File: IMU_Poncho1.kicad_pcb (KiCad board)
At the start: 2 copper layers, 41 x 61 mm, 11 parts, among them J1 Conn_01x06_Female, U1 MPU-9250

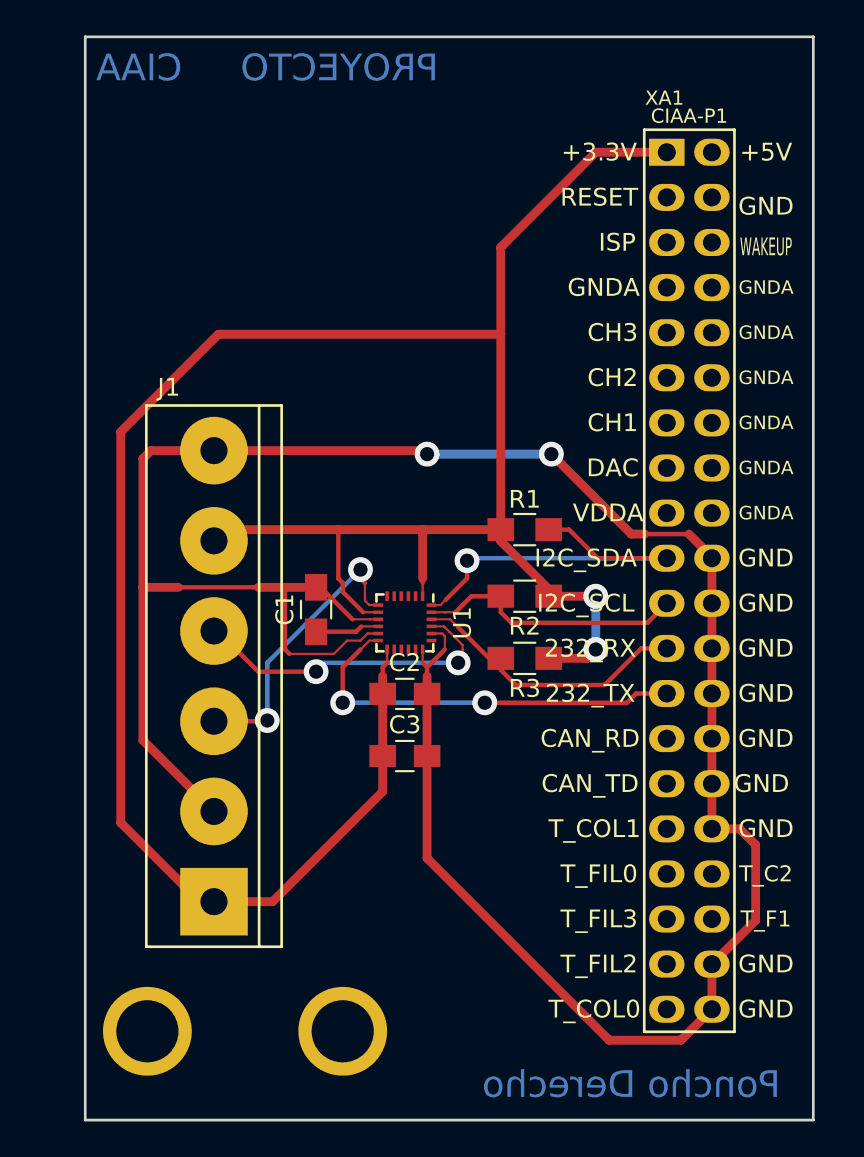
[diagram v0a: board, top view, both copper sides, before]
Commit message: Correccion del conector del barometro y se lo coloca separado del IMU. Dibujo 3D
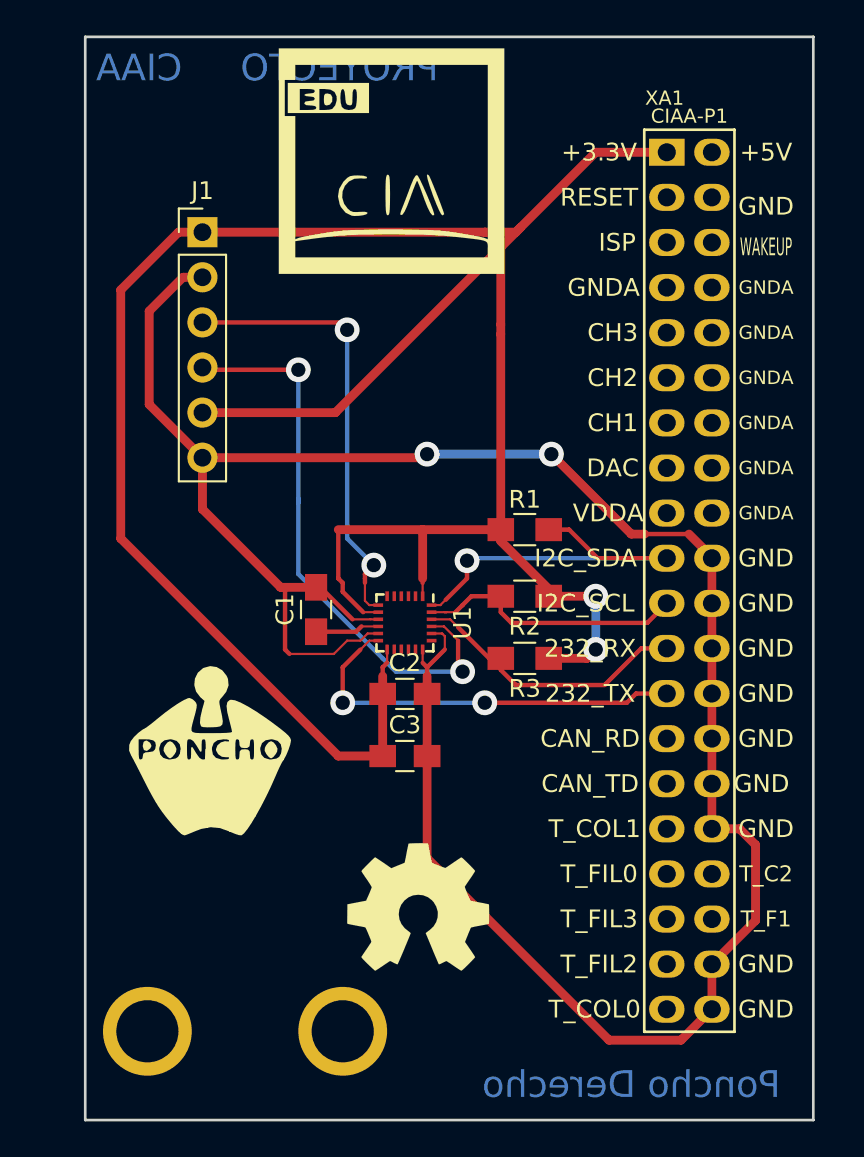
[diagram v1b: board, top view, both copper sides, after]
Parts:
- added G1: LOGO, Poncho_Esqueleto:Logo_Poncho, F.Cu at (132.5, 125.2)
- added G2: Logo_OSHWA, Poncho_Esqueleto:Logo_OSHWA, F.Cu at (144.2, 134.0)
- added G3: Logo_EDU-CIAA, Poncho_Esqueleto:Logo_EDU-CIAA, F.Cu at (142.8, 92.0)
- J1: footprint Poncho_Modelos:bornier6 -> Pin_Headers:Pin_Header_Straight_1x06_Pitch2.54mm
- moved J1 25.0 mm to (132.1, 96.0), turned to 0 degrees
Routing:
- net Net-(J1-Pad4): track 18.3 -> 32.4 mm
- net GND: track 143.9 -> 133.6 mm
- net Net-(J1-Pad3): track 16.4 -> 25.3 mm
- net +3V3: track 140.0 -> 144.4 mm
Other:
- net class Default: clearance 0.2 -> 0.125
- rule trace_clearance: 0.2 -> 0.125

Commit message: Corrigiendo seguimiento de archivos, borrando del grupo
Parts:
- added REF**: Fiducial_Modern_CopperTop, Fiducials:Fiducial_Modern_CopperTop, F.Cu at (133.0, 92.0)
- added REF**: Fiducial_Modern_CopperTop, Fiducials:Fiducial_Modern_CopperTop, F.Cu at (149.0, 141.0)
- moved G1 7.29 mm to (131.8, 132.5)
- moved G2 1.80 mm to (142.8, 133.0)
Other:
- board text added: "Barometro"
- board text added: "Navegador Inercial"
- board text added: "Navegador_Inercial"
- board text removed: "Poncho Derecho"
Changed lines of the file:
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@@
     (area 125.424999 84.924999 166.575001 146.075001)
     (thickness 1.6)
-    (drawings 8)
+    (drawings 10)
     (tracks 171)
     (zones 0)
-    (modules 14)
+    (modules 16)
     (nets 38)
   )
@@
   )
   (setup
-    (last_trace_width 0.5)
+    (last_trace_width 0.25)
     (user_trace_width 0.125)
     (user_trace_width 0.25)
@@
   )
   (module Poncho_Esqueleto:Logo_OSHWA (layer F.Cu)
-    (at 144.25 134)
+    (at 142.75 133)
     (fp_text reference G2 (at 0 4.2418) (layer F.SilkS) hide
       (effects (font (size 0.7112 0.4572) (thickness 0.1143)))
@@
   )
   (module Poncho_Esqueleto:Logo_Poncho (layer F.Cu)
-    (at 132.5 125.25)
+    (at 131.75 132.5)
     (fp_text reference G1 (at 0.127 5.588) (layer F.SilkS) hide
       (effects (font (thickness 0.3)))
@@
     )
   )
+  (module Fiducials:Fiducial_Modern_CopperTop (layer F.Cu)
+    (at 133 92)
+    (descr "Fiducial, Modern, Copper Top, Passermarke,")
+    (tags "Fiducial, Modern, Copper Top, Passermarke,")
+    (fp_text reference REF** (at 0.03048 -4.26974) (layer F.SilkS)
+      (effects (font (size 1 1) (thickness 0.15)))
+    )
+    (fp_text value Fiducial_Modern_CopperTop (at 0.81026 4.18084) (layer F.Fab)
+      (effects (font (size 1 1) (thickness 0.15)))
+    )
+    (fp_circle (center 0 0) (end 1.52908 0) (layer F.Cu) (width 0.381))
+    (fp_circle (center 0 0) (end 1.7907 0) (layer F.Cu) (width 0.381))
+    (pad ~ smd circle (at 0 0) (size 4.8006 4.8006) (layers F.Mask)
+      (solder_mask_margin 2.99974))
+  )
+  (module Fiducials:Fiducial_Modern_CopperTop (layer F.Cu)
+    (at 149 141)
+    (descr "Fiducial, Modern, Copper Top, Passermarke,")
+    (tags "Fiducial, Modern, Copper Top, Passermarke,")
+    (fp_text reference REF** (at 0.03048 -4.26974) (layer F.SilkS)
+      (effects (font (size 1 1) (thickness 0.15)))
+    )
+    (fp_text value Fiducial_Modern_CopperTop (at 0.81026 4.18084) (layer F.Fab)
+      (effects (font (size 1 1) (thickness 0.15)))
+    )
+    (fp_circle (center 0 0) (end 1.52908 0) (layer F.Cu) (width 0.381))
+    (fp_circle (center 0 0) (end 1.7907 0) (layer F.Cu) (width 0.381))
+    (pad ~ smd circle (at 0 0) (size 4.8006 4.8006) (layers F.Mask)
+      (solder_mask_margin 2.99974))
+  )
+  (gr_text Barometro (at 142.25 106) (layer F.SilkS)
+    (effects (font (size 1.5 1.5) (thickness 0.3)))
+  )
+  (gr_text "Navegador Inercial" (at 154.25 143.25) (layer F.SilkS)
+    (effects (font (size 1.5 1.5) (thickness 0.3)))
+  )
   (dimension 60.8 (width 0.3) (layer Dwgs.User)
     (gr_text "60,800 mm" (at 171.85 115.6 270) (layer Dwgs.User)
@@
     (effects (font (size 1.5 1.5) (thickness 0.3)) (justify mirror))
   )
-  (gr_text "Poncho Derecho" (at 156.25 144) (layer B.Cu)
+  (gr_text Navegador_Inercial (at 154.25 143.5) (layer B.Cu)
     (effects (font (size 1.5 1.5) (thickness 0.3)) (justify mirror))
   )
@@
   (segment (start 140.75 118.5) (end 138.5 118.5) (width 0.25) (layer F.Cu) (net 1))
   (segment (start 141.05 118.2) (end 140.75 118.5) (width 0.25) (layer F.Cu) (net 1))
+  (segment (start 137 119.75) (end 139.75 119.75) (width 0.25) (layer F.Cu) (net 2))
+  (segment (start 141.4 118.6) (end 141 119) (width 0.125) (layer F.Cu) (net 2))
+  (segment (start 137 119.75) (end 136.75 119.5) (width 0.25) (layer F.Cu) (net 2))
+  (segment (start 136.75 116) (end 136.75 119.5) (width 0.25) (layer F.Cu) (net 2))
+  (segment (start 141.4 118.6) (end 142 118.6) (width 0.125) (layer F.Cu) (net 2))
+  (segment (start 140.5 119) (end 141 119) (width 0.25) (layer F.Cu) (net 2))
+  (segment (start 139.75 119.75) (end 140.5 119) (width 0.25) (layer F.Cu) (net 2))
   (segment (start 136.75 116) (end 136.5 116) (width 0.5) (layer F.Cu) (net 2))
   (segment (start 132.1 111.6) (end 132.1 108.7) (width 0.5) (layer F.Cu) (net 2))
@@
   (segment (start 144.7 108.3) (end 144.75 108.35) (width 0.5) (layer F.Cu) (net 2))
   (segment (start 160.79 114.29) (end 160.79 114.36) (width 0.5) (layer F.Cu) (net 2) (status 30))
-  (segment (start 142 118.6) (end 141.4 118.6) (width 0.125) (layer F.Cu) (net 2))
-  (segment (start 136.75 119.5) (end 136.75 116) (width 0.25) (layer F.Cu) (net 2))
-  (segment (start 137 119.75) (end 136.75 119.5) (width 0.25) (layer F.Cu) (net 2))
-  (segment (start 139.5 119.75) (end 137 119.75) (width 0.125) (layer F.Cu) (net 2))
-  (segment (start 140.25 119) (end 139.5 119.75) (width 0.125) (layer F.Cu) (net 2))
-  (segment (start 141 119) (end 140.25 119) (width 0.125) (layer F.Cu) (net 2))
-  (segment (start 141.4 118.6) (end 141 119) (width 0.125) (layer F.Cu) (net 2))
   (segment (start 141.55 117.8) (end 140.55 117.8) (width 0.125) (layer F.Cu) (net 2))
   (segment (start 142 117.8) (end 141.55 117.8) (width 0.125) (layer F.Cu) (net 2))

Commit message: Reconstruyendo archivos
Colocando los archivos que se abrieron a otra rama
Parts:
- removed REF** (x2): Fiducial_Modern_CopperTop, Fiducials:Fiducial_Modern_CopperTop
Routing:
- net +3V3: track 144.4 -> 142.8 mm
- net GND: track 133.6 -> 134.5 mm
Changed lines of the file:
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@@
     (thickness 1.6)
     (drawings 10)
-    (tracks 171)
+    (tracks 175)
     (zones 0)
-    (modules 16)
+    (modules 14)
     (nets 38)
   )
@@
   )
   (setup
-    (last_trace_width 0.25)
+    (last_trace_width 0.5)
     (user_trace_width 0.125)
     (user_trace_width 0.25)
@@
     )
   )
-  (module Fiducials:Fiducial_Modern_CopperTop (layer F.Cu)
-    (at 133 92)
-    (descr "Fiducial, Modern, Copper Top, Passermarke,")
-    (tags "Fiducial, Modern, Copper Top, Passermarke,")
-    (fp_text reference REF** (at 0.03048 -4.26974) (layer F.SilkS)
-      (effects (font (size 1 1) (thickness 0.15)))
-    )
-    (fp_text value Fiducial_Modern_CopperTop (at 0.81026 4.18084) (layer F.Fab)
-      (effects (font (size 1 1) (thickness 0.15)))
-    )
-    (fp_circle (center 0 0) (end 1.52908 0) (layer F.Cu) (width 0.381))
-    (fp_circle (center 0 0) (end 1.7907 0) (layer F.Cu) (width 0.381))
-    (pad ~ smd circle (at 0 0) (size 4.8006 4.8006) (layers F.Mask)
-      (solder_mask_margin 2.99974))
-  )
-  (module Fiducials:Fiducial_Modern_CopperTop (layer F.Cu)
-    (at 149 141)
-    (descr "Fiducial, Modern, Copper Top, Passermarke,")
-    (tags "Fiducial, Modern, Copper Top, Passermarke,")
-    (fp_text reference REF** (at 0.03048 -4.26974) (layer F.SilkS)
-      (effects (font (size 1 1) (thickness 0.15)))
-    )
-    (fp_text value Fiducial_Modern_CopperTop (at 0.81026 4.18084) (layer F.Fab)
-      (effects (font (size 1 1) (thickness 0.15)))
-    )
-    (fp_circle (center 0 0) (end 1.52908 0) (layer F.Cu) (width 0.381))
-    (fp_circle (center 0 0) (end 1.7907 0) (layer F.Cu) (width 0.381))
-    (pad ~ smd circle (at 0 0) (size 4.8006 4.8006) (layers F.Mask)
-      (solder_mask_margin 2.99974))
-  )
   (gr_text Barometro (at 142.25 106) (layer F.SilkS)
     (effects (font (size 1.5 1.5) (thickness 0.3)))
@@
   (segment (start 140.75 118.5) (end 138.5 118.5) (width 0.25) (layer F.Cu) (net 1))
   (segment (start 141.05 118.2) (end 140.75 118.5) (width 0.25) (layer F.Cu) (net 1))
+  (segment (start 160.79 137.22) (end 162.22 137.22) (width 0.5) (layer F.Cu) (net 2))
+  (segment (start 162.35 129.6) (end 163.25 130.5) (width 0.5) (layer F.Cu) (net 2))
+  (segment (start 163.25 130.5) (end 163.25 134.76) (width 0.5) (layer F.Cu) (net 2))
+  (segment (start 162.35 129.6) (end 160.79 129.6) (width 0.5) (layer F.Cu) (net 2) (status 10))
+  (segment (start 163.19 134.82) (end 163.25 134.76) (width 0.5) (layer F.Cu) (net 2))
+  (segment (start 163.19 136.25) (end 163.19 134.82) (width 0.5) (layer F.Cu) (net 2))
+  (segment (start 162.22 137.22) (end 163.19 136.25) (width 0.5) (layer F.Cu) (net 2))
   (segment (start 137 119.75) (end 139.75 119.75) (width 0.25) (layer F.Cu) (net 2))
   (segment (start 141.4 118.6) (end 141 119) (width 0.125) (layer F.Cu) (net 2))
@@
   (segment (start 144.75 131.25) (end 155 141.5) (width 0.5) (layer F.Cu) (net 2))
   (segment (start 144.75 125.5) (end 144.75 122) (width 0.5) (layer F.Cu) (net 2))
-  (segment (start 160.79 129.6) (end 162.35 129.6) (width 0.5) (layer F.Cu) (net 2) (status 10))
-  (segment (start 163.25 134.76) (end 160.79 137.22) (width 0.5) (layer F.Cu) (net 2) (status 20))
-  (segment (start 163.25 130.5) (end 163.25 134.76) (width 0.5) (layer F.Cu) (net 2))
-  (segment (start 162.35 129.6) (end 163.25 130.5) (width 0.5) (layer F.Cu) (net 2))
   (segment (start 160.79 129.6) (end 160.79 127.06) (width 0.5) (layer F.Cu) (net 2) (status 30))
   (segment (start 160.79 127.06) (end 160.79 124.52) (width 0.5) (layer F.Cu) (net 2) (status 30))
@@
   (segment (start 160.79 116.9) (end 160.79 114.36) (width 0.5) (layer F.Cu) (net 2) (status 30))
   (segment (start 160.79 139.76) (end 160.79 137.22) (width 0.5) (layer F.Cu) (net 2) (status 30))
+  (segment (start 141.25 117.4) (end 141.15 117.4) (width 0.25) (layer F.Cu) (net 3))
+  (segment (start 141.15 117.4) (end 140.25 116.5) (width 0.25) (layer F.Cu) (net 3))
+  (segment (start 141.75 112.75) (end 144.5 112.75) (width 0.5) (layer F.Cu) (net 3))
+  (segment (start 140.25 114.25) (end 141.75 112.75) (width 0.5) (layer F.Cu) (net 3))
+  (segment (start 140.25 114.75) (end 140.25 114.25) (width 0.5) (layer F.Cu) (net 3))
+  (segment (start 140.25 116.5) (end 140.25 114.75) (width 0.5) (layer F.Cu) (net 3))
   (segment (start 148 96) (end 149.75 96) (width 0.5) (layer F.Cu) (net 3))
   (segment (start 149.75 96) (end 150 95.75) (width 0.5) (layer F.Cu) (net 3))
@@
   (via (at 154.25 119.5) (size 1.4) (drill 0.8) (layers F.Cu B.Cu) (net 3))
   (segment (start 153.75 120) (end 154.25 119.5) (width 0.5) (layer F.Cu) (net 3))
-  (segment (start 142 117.4) (end 141.15 117.4) (width 0.125) (layer F.Cu) (net 3))
-  (segment (start 139.75 115.5) (end 139.75 112.75) (width 0.25) (layer F.Cu) (net 3))
-  (segment (start 140 115.75) (end 139.75 115.5) (width 0.25) (layer F.Cu) (net 3))
-  (segment (start 140 116.25) (end 140 115.75) (width 0.25) (layer F.Cu) (net 3))
-  (segment (start 141.15 117.4) (end 140 116.25) (width 0.25) (layer F.Cu) (net 3))
+  (segment (start 142 117.4) (end 141.25 117.4) (width 0.125) (layer F.Cu) (net 3))
   (segment (start 144.5 116.5) (end 144.5 115.75) (width 0.125) (layer F.Cu) (net 3))
   (segment (start 144.5 115.5) (end 144.5 112.75) (width 0.5) (layer F.Cu) (net 3))
@@
   (segment (start 151.6 116.1) (end 151.6 116.5) (width 0.5) (layer F.Cu) (net 3))
   (segment (start 148.9 112.75) (end 144.5 112.75) (width 0.5) (layer F.Cu) (net 3))
-  (segment (start 144.5 112.75) (end 139.75 112.75) (width 0.5) (layer F.Cu) (net 3))
   (segment (start 148.9 112.75) (end 148.9 101.75) (width 0.5) (layer F.Cu) (net 3))
   (segment (start 148.9 101.75) (end 148.9 101.2) (width 0.5) (layer F.Cu) (net 3))
@@
   (via (at 146.75 120.75) (size 1.4) (drill 0.8) (layers F.Cu B.Cu) (net 5))
   (segment (start 146.5 120.5) (end 146.75 120.75) (width 0.25) (layer F.Cu) (net 5))
-  (segment (start 137.5 111.25) (end 137.5 111) (width 0.25) (layer B.Cu) (net 5) (status 2))
+  (segment (start 137.5 111.25) (end 137.5 111) (width 0.25) (layer B.Cu) (net 5))
   (segment (start 145 117) (end 145.5 117) (width 0.125) (layer F.Cu) (net 6))
   (segment (start 147 115.25) (end 147 114.5) (width 0.25) (layer F.Cu) (net 6))
